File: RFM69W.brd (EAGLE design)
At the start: 25.4 x 34.3 mm, 18 parts, among them U1 RFM69W, U2 MCP1701

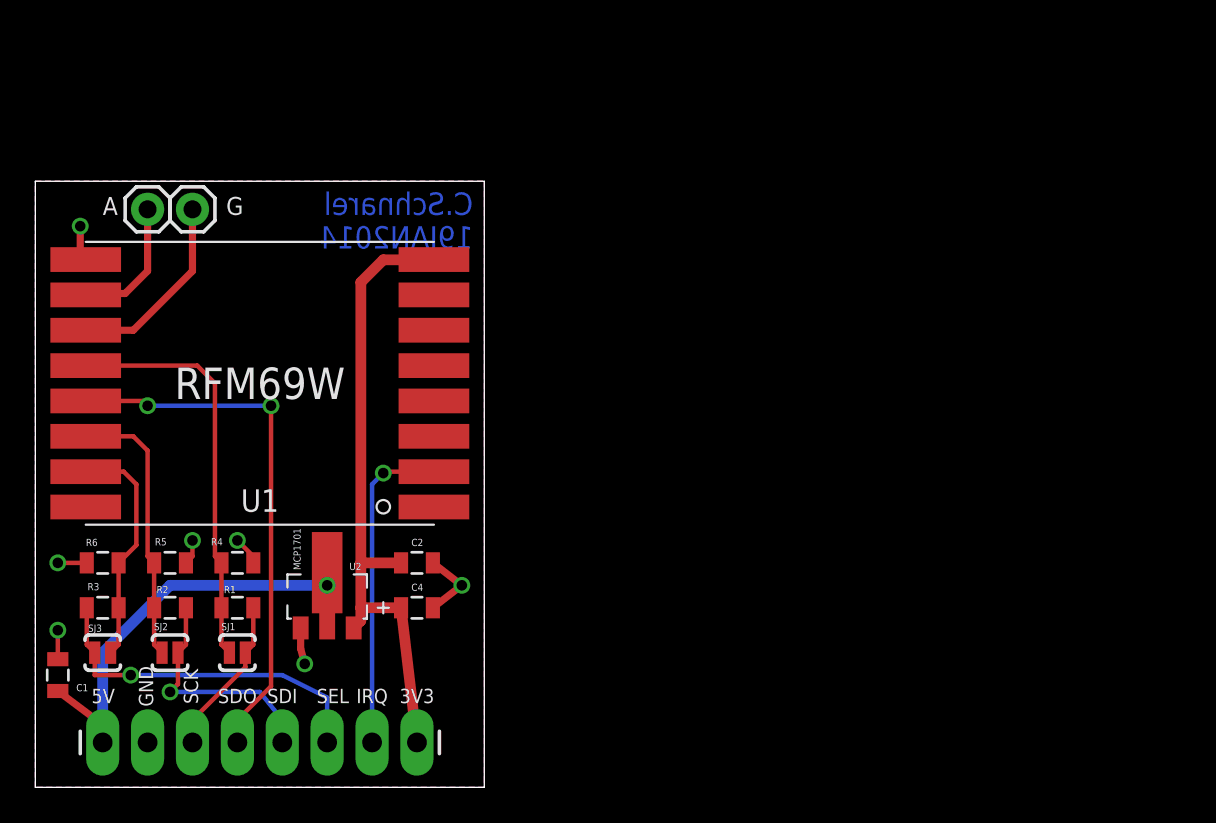
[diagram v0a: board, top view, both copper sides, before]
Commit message: Combo Arduino Pro Mini and RFM69W
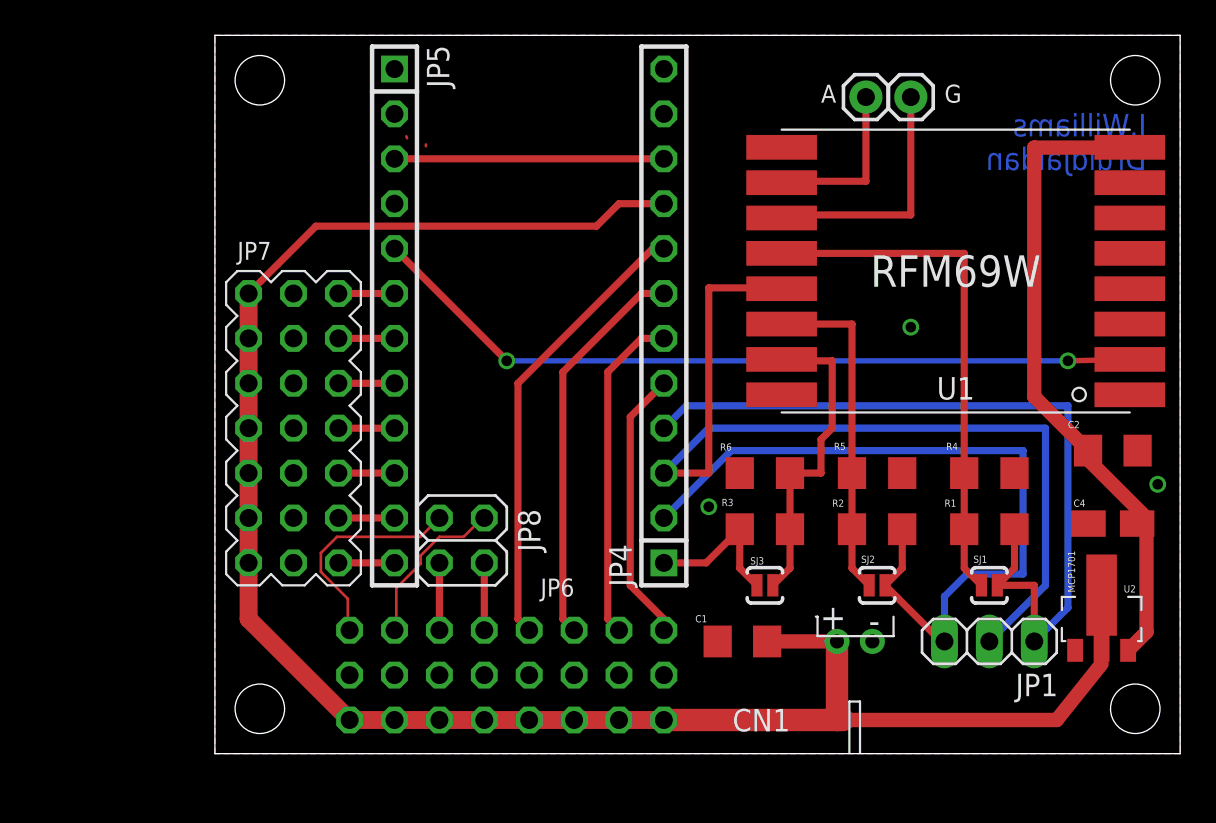
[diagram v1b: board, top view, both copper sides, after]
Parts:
- added CN1: +5v, adafruit:JST-PH-2-THM-RA
- added JP4, JP5: (no value), pinhead:1X12
- added JP6: PIN_3X8, pinhead_3row:PIN_3X8
- added JP7: PIN_3X7, pinhead_3row:PIN_3X7
- added JP8: (no value), pinhead:2X02
- C1, C2: device SparkFun-Capacitors:0805 -> rcl:C1206
- C4: device ChipsParts:0805-POL -> resistor:A/3216-18R
- JP1: device SparkFun-Connectors:1X08_LONGPADS -> pinhead:1X03
- R1, R2, R3, R4, R5, R6: device SparkFun-Resistors:0805 -> resistor:R1206
- moved JP1 50.5 mm to (54.0, 8.26), turned to 180 degrees
- moved U2 43.8 mm to (60.3, 9.53)
- moved R4 42.8 mm to (54.0, 17.8)
- moved R1 42.8 mm to (54.0, 14.6)
- moved SJ1 42.7 mm to (54.0, 11.4)
- moved JP2 41.1 mm to (47.0, 39.1)
- moved JP3 41.1 mm to (49.5, 39.1)
- moved R5 40.3 mm to (47.6, 17.8)
- moved R2 40.3 mm to (47.6, 14.6)
- moved SJ2 40.2 mm to (47.6, 11.4)
- moved C2 39.9 mm to (61.0, 19.1)
- moved U1 39.9 mm to (52.1, 29.2)
- moved C4 39.7 mm to (61.0, 14.9)
- moved C1 38.8 mm to (40.0, 8.26), turned to 180 degrees
- moved R6 37.8 mm to (41.3, 17.8)
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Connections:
- removed net N$2: C1.1, JP1.1, U2.2
- removed net N$3: JP1.4, U1.13
- removed net N$4: JP1.7, U1.2
- removed net N$6: JP1.3, R1.2, SJ1.2
- removed net N$7: JP1.5, R2.2, SJ2.2
- removed net N$9: JP1.6, R3.2, SJ3.2
- removed net VCC: C2.1, C4.1, JP1.8, U1.8, U2.3
- new net +3V3: C2.1, C4.+, U1.8, U2.3
- new net +5V: C1.1, CN1.1, JP4.9, JP6.17, JP6.18, JP6.19, JP6.20, JP6.21, JP6.22, JP6.23, JP6.24, JP7.15, JP7.16, JP7.17, JP7.18, JP7.19, JP7.20, JP7.21, U2.2
- new net A0: JP4.5, JP6.1
- new net A1: JP4.6, JP6.2
- new net A2: JP4.7, JP6.3
- new net A3: JP4.8, JP6.4
- new net A4: JP6.5, JP8.1
- new net A5: JP6.6, JP8.2
- new net A6: JP6.7, JP8.3
- new net A7: JP6.8, JP8.4
- new net D10: JP4.1, R3.2, SJ3.2
- new net D2: JP5.5, U1.2
- new net D3: JP5.6, JP7.1
- new net D4: JP5.7, JP7.2
- new net D5: JP5.8, JP7.3
- new net D6: JP5.9, JP7.4
- new net D7: JP5.10, JP7.5
- new net D8: JP5.11, JP7.6
- new net D9: JP5.12, JP7.7
- new net MISO: JP1.2, JP4.3, U1.13
- new net MOSI: JP1.3, JP4.2, R2.2, SJ2.2
- new net RAW: JP4.12
- new net RST: JP4.10, JP5.3
- new net RX1: JP5.2
- new net SCK: JP1.1, JP4.4, R1.2, SJ1.2
- new net TX1: JP5.1
- net GND: now also C4.-, CN1.2, JP4.11, JP5.4, JP6.10, JP6.11, JP6.12, JP6.13, JP6.14, JP6.15, JP6.16, JP6.9, JP7.10, JP7.11, JP7.12, JP7.13, JP7.14, JP7.8, JP7.9; no longer C4.2, JP1.2
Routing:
- net +5V: track 0.00 -> 107.2 mm
- net MISO: track 0.00 -> 53.2 mm
- net SCK: track 0.00 -> 46.4 mm
- net MOSI: track 0.00 -> 44.6 mm
- net D2: track 0.00 -> 44.3 mm, vias 0 -> 2
- net +3V3: track 0.00 -> 37.6 mm
- net VCC: track 36.7 -> 0.00 mm
- net N$3: track 30.4 -> 0.00 mm, vias 2 -> 0
- net A3: track 0.00 -> 25.6 mm
- net N$2: track 23.5 -> 0.00 mm, vias 1 -> 0
- net A2: track 0.00 -> 22.4 mm
- net N$9: track 20.0 -> 0.00 mm, vias 1 -> 0
- net A1: track 0.00 -> 18.8 mm
- net N$4: track 18.4 -> 0.00 mm, vias 1 -> 0
- net A0: track 0.00 -> 15.5 mm
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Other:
- board size 25.4 x 34.3 mm -> 54.6 x 40.6 mm
- board text added: "J.Williams DruidJaidan"
- board text removed: "3V3"
- board text removed: "5V"
- board text removed: "C.Schnarel 19JAN2014"
- board text removed: "GND"
- board text removed: "IRQ"
- board text removed: "SCK"
- board text removed: "SDI"
- board text removed: "SDO"
- board text removed: "SEL"
